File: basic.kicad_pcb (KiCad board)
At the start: 4 copper layers, 50.5 x 100 mm, 147 parts, among them CON1 MSATA-PCIE_MINI-CARD-MM60-52B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, J1 Conn_02x02_Top_Bottom, J2 Conn_01x02_Male, J3 Conn_01x02_Male, J4 simcard, Q1 MBT3904DW1, Q2 MMUN2233LT1G, Q3 MMUN2233LT1G, SW1 SW_Push, U1 TLV76750, U10 TC2030_SWD, U12 TPS22810DRV, U13 USBLC6-4SC6, U2 AP63203WU, U3 MCP73123-22S, U4 LM73100, U5 LM73100, U6 MCP2515-QFN, U7 TCAN332, U8 MMA8452Q, U9 ESP32-WROOM-32U, X1 dummy, X2 dummy, Y1 M8AIG-16-12-2T3

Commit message: PCB Design completed.
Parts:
- moved R40 24.6 mm to (84.2, 66.0), turned to 180 degrees
- moved C55 23.8 mm to (84.2, 64.7), turned to 180 degrees
- moved R41 17.3 mm to (89.4, 68.8), turned to 270 degrees
- moved C57 16.7 mm to (86.5, 68.2), turned to 180 degrees
- moved R42 15.9 mm to (90.8, 68.8), turned to 270 degrees
- moved C53 14.8 mm to (90.9, 66.7)
- moved C51 14.5 mm to (91.0, 64.8)
- moved D3 1.65 mm to (70.6, 58.5)
- moved U13 1.38 mm to (87.7, 65.8)
- moved U10 1.00 mm to (94.4, 112.2)
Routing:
- net GND: track 171.8 -> 272.2 mm, vias 137 -> 246
- net /modem/sim_vcc: track 0.00 -> 73.2 mm, vias 0 -> 1
- net Net-(CON1-Pad10): track 0.00 -> 68.6 mm, vias 0 -> 1
- net Net-(CON1-Pad12): track 0.00 -> 56.7 mm, vias 0 -> 1
- net Net-(CON1-Pad14): track 0.00 -> 55.2 mm, vias 0 -> 1
- net /modem/sim_clk: track 0.00 -> 7.78 mm
- net /modem/sim_reset: track 0.00 -> 6.92 mm
- net /modem/sim_data: track 0.00 -> 5.19 mm
- net CANH: track 15.1 -> 18.2 mm
- net CANL: track 17.1 -> 19.7 mm
- net /esp32/MODEM_RX: track 45.2 -> 46.7 mm
- net /esp32/MODEM_TX: track 39.1 -> 39.9 mm
- net Net-(R29-Pad2): track 4.81 -> 4.14 mm
- net /esp32/SENSE_V12: track 9.63 -> 10.2 mm
- net CPU_ENABLE: track 37.7 -> 37.6 mm, vias 2 -> 4
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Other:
- board size 50.5 x 100 mm -> 50.5 x 80 mm
- rule trace_min: 0.127 -> 0.2
- board text removed: "Battery Pack Dimension : 30x54mm"
- board text removed: "Ground Polygons!"

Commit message: Fixed DRC Errors.
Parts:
- U4, U5: value LM73100 -> RPW0010A
- moved X2 85.9 mm to (75.0, 59.0)
- moved X1 85.7 mm to (79.0, 59.0)
- moved Q3 0.20 mm to (76.2, 110.5)
- moved FB1 0.15 mm to (67.0, 90.5)
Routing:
- net GND: track 272.2 -> 322.2 mm, vias 246 -> 250
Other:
- board text added: "REV 1.0 03-21"

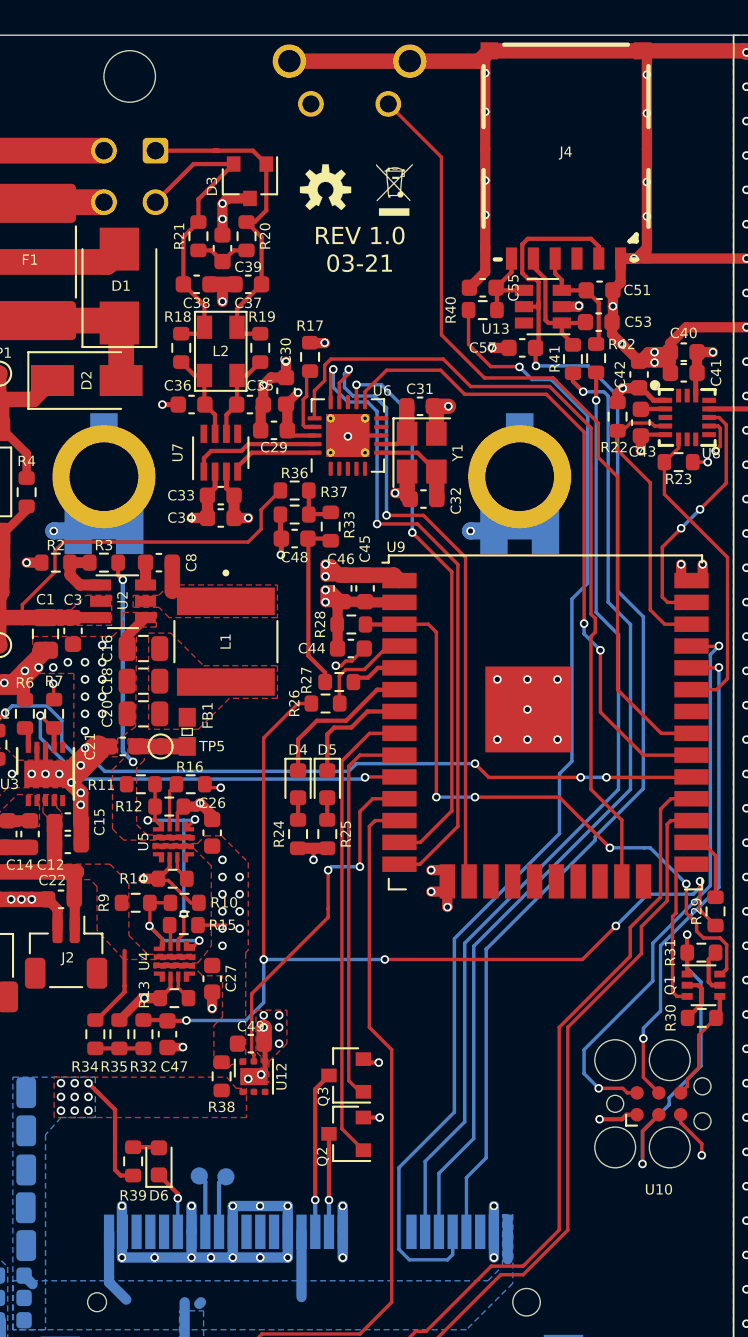
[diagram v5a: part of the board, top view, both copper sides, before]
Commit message: Changed MCU connection.
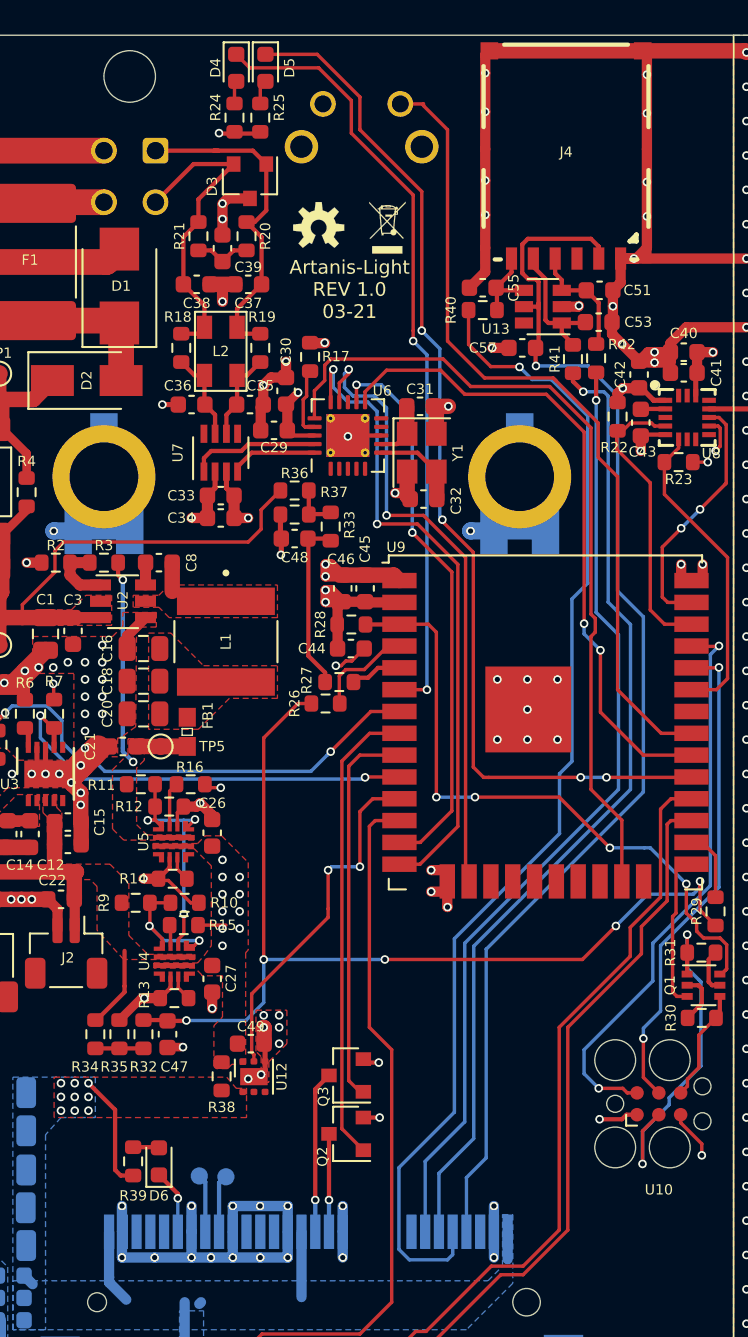
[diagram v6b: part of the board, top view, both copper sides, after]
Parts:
- U4, U5: value RPW0010A -> LM73100
- moved R25 41.9 mm to (71.2, 54.8)
- moved R24 41.9 mm to (69.7, 54.8)
- moved D4 41.9 mm to (69.8, 51.9)
- moved D5 41.9 mm to (71.5, 51.9)
- moved X1 2.24 mm to (78.6, 61.2)
- moved X2 2.24 mm to (74.6, 61.2)
- moved SW1 0.70 mm to (77.1, 54.0), turned to 0 degrees
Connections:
- SW1 pad 1: softreset -> GND
- SW1 pad 2: GND -> softreset
- U9 pad 29: /esp32/CHARGER_EN -> /esp32/LED_BLUE
- U9 pad 7: /esp32/LED_BLUE -> /esp32/CHARGER_EN
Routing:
- net /esp32/LED_BLUE: track 6.87 -> 61.3 mm, vias 0 -> 4
- net /esp32/LED_GREEN: track 8.92 -> 45.5 mm, vias 0 -> 2
- net /esp32/CHARGER_EN: track 45.5 -> 29.4 mm, vias 4 -> 2
- net GND: track 322.2 -> 310.3 mm
- net +3V3: track 36.0 -> 34.5 mm
- net softreset: track 47.5 -> 48.0 mm
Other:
- board text added: "Artanis-Light REV 1.0 03-21"
- board text removed: "REV 1.0 03-21"

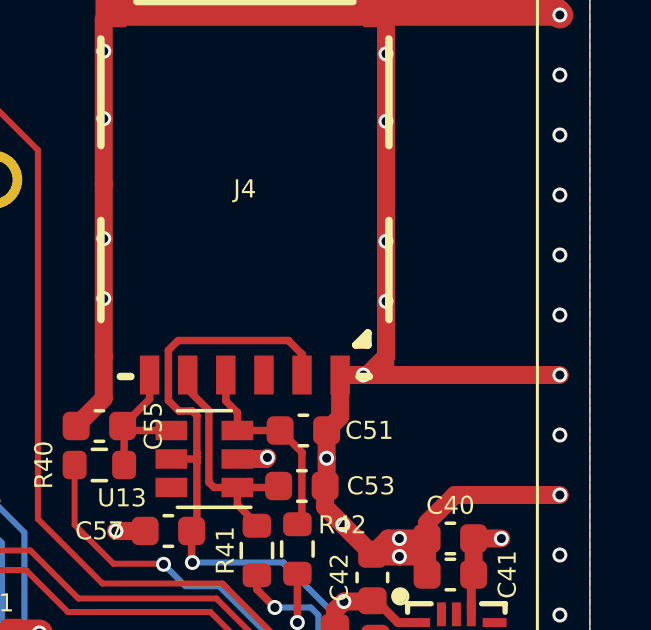
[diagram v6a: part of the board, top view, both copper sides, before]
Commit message: Added cutout for antenna cable.
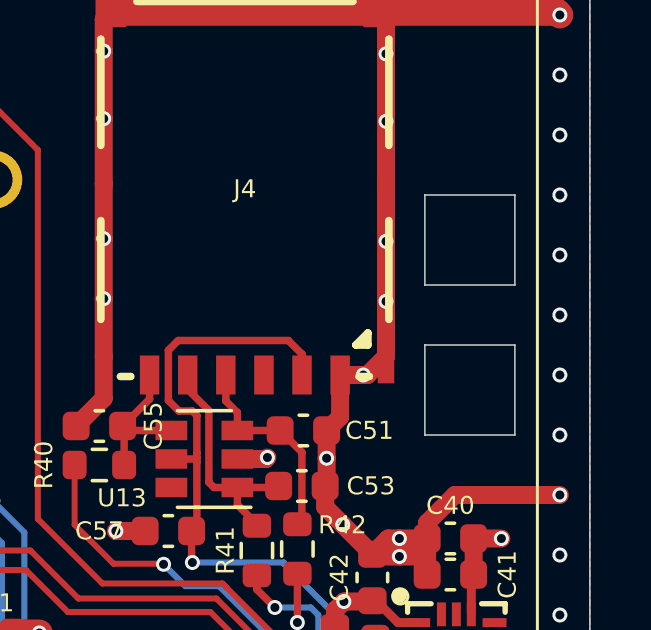
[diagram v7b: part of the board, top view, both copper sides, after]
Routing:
- net GND: track 310.3 -> 303.0 mm
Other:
- outline, holes or cut-outs redrawn
